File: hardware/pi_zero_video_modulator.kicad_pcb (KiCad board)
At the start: 2 copper layers, 65 x 30 mm, 47 parts, among them J1 RPi_GPIO, J2 Pi Video, J3 RF OUT, SW1 SW_SPDT, U1 NJM2519A, X1 F88SM

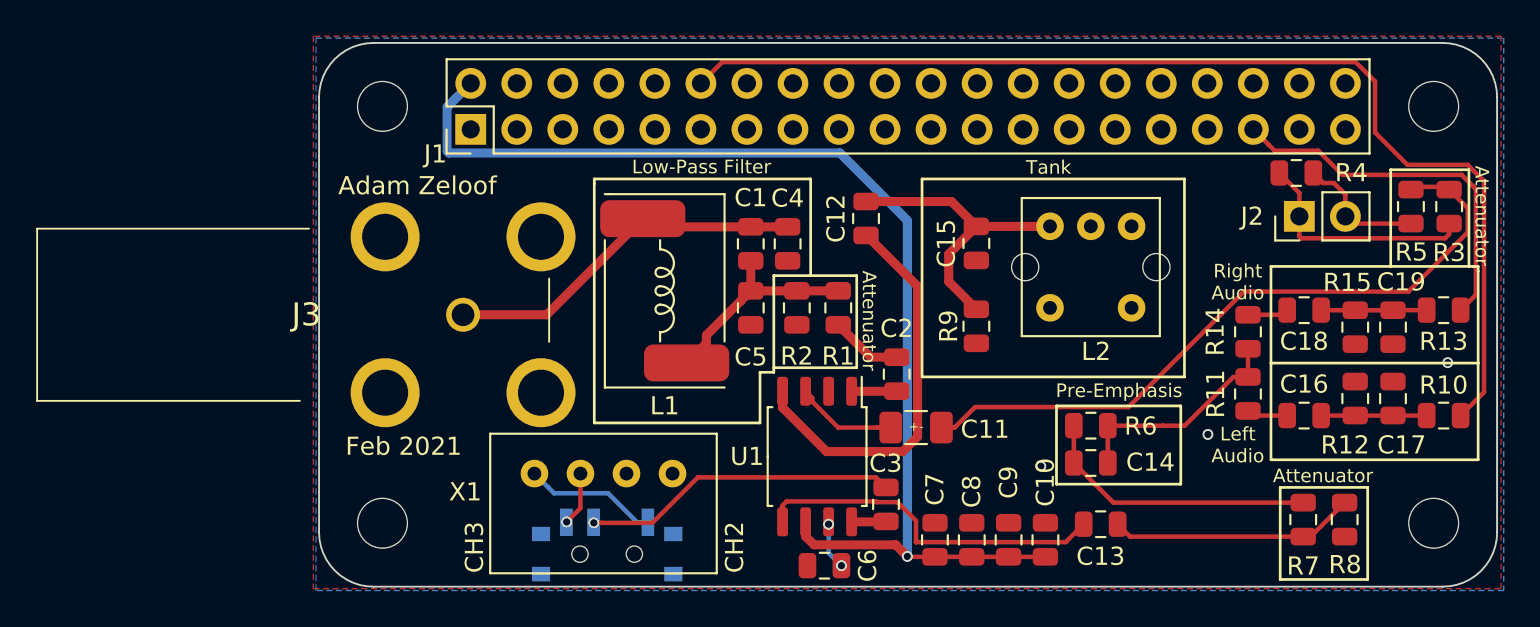
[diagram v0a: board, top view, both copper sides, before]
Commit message: Changed board profile and F connector
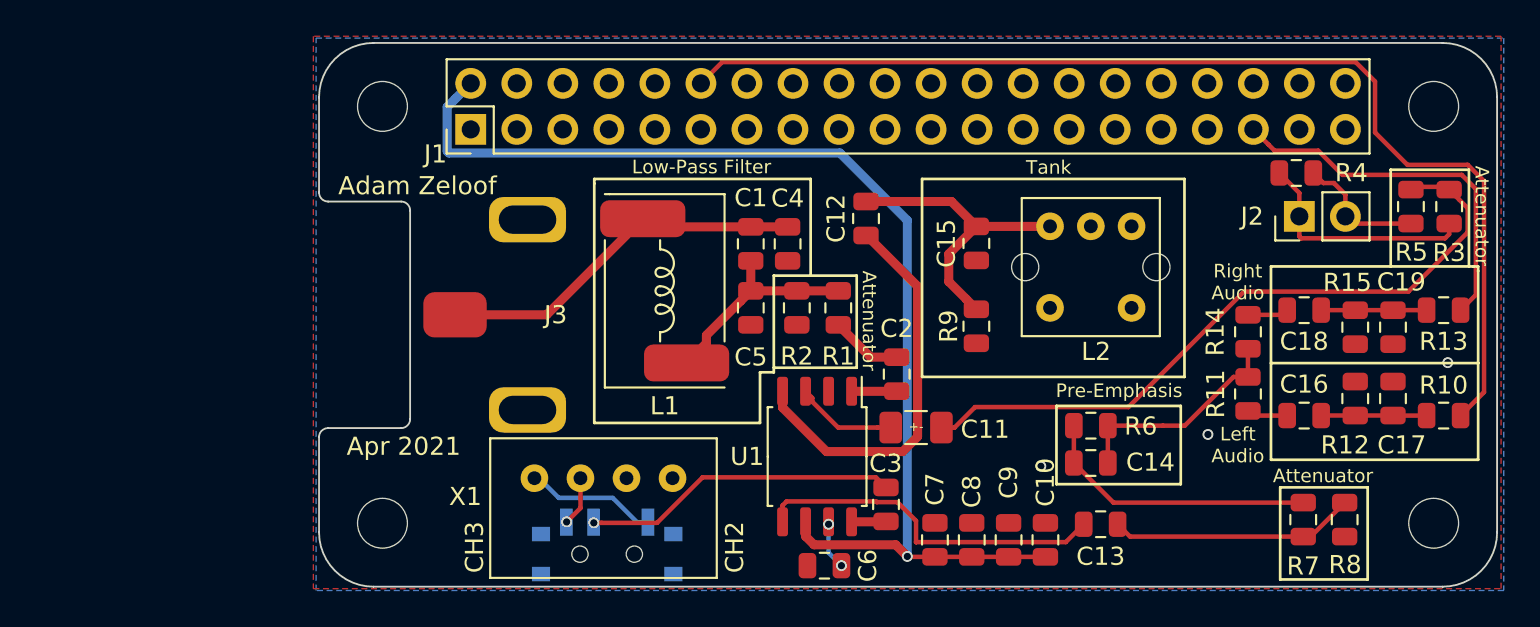
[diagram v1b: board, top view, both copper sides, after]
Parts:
- J3: value RF OUT -> Amphenol 531-40101; footprint KiCad_More:733300030 -> rf_modulator:Amphenol-531-40101
- moved J3 3.56 mm to (24.0, 39.5), turned to 0 degrees
- moved G*** 1.46 mm to (45.5, 39.5)
- moved X1 0.25 mm to (24.4, 48.5)
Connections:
- J3 pad 1: RF_OUT -> GND
- J3 pad 3: (no net) -> RF_OUT
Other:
- outline, holes or cut-outs redrawn
- board text added: "Apr 2021"
- board text removed: "Feb 2021"
